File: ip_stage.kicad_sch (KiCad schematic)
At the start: 21 parts, among them J10 XH, J11 XH, U4 TL072

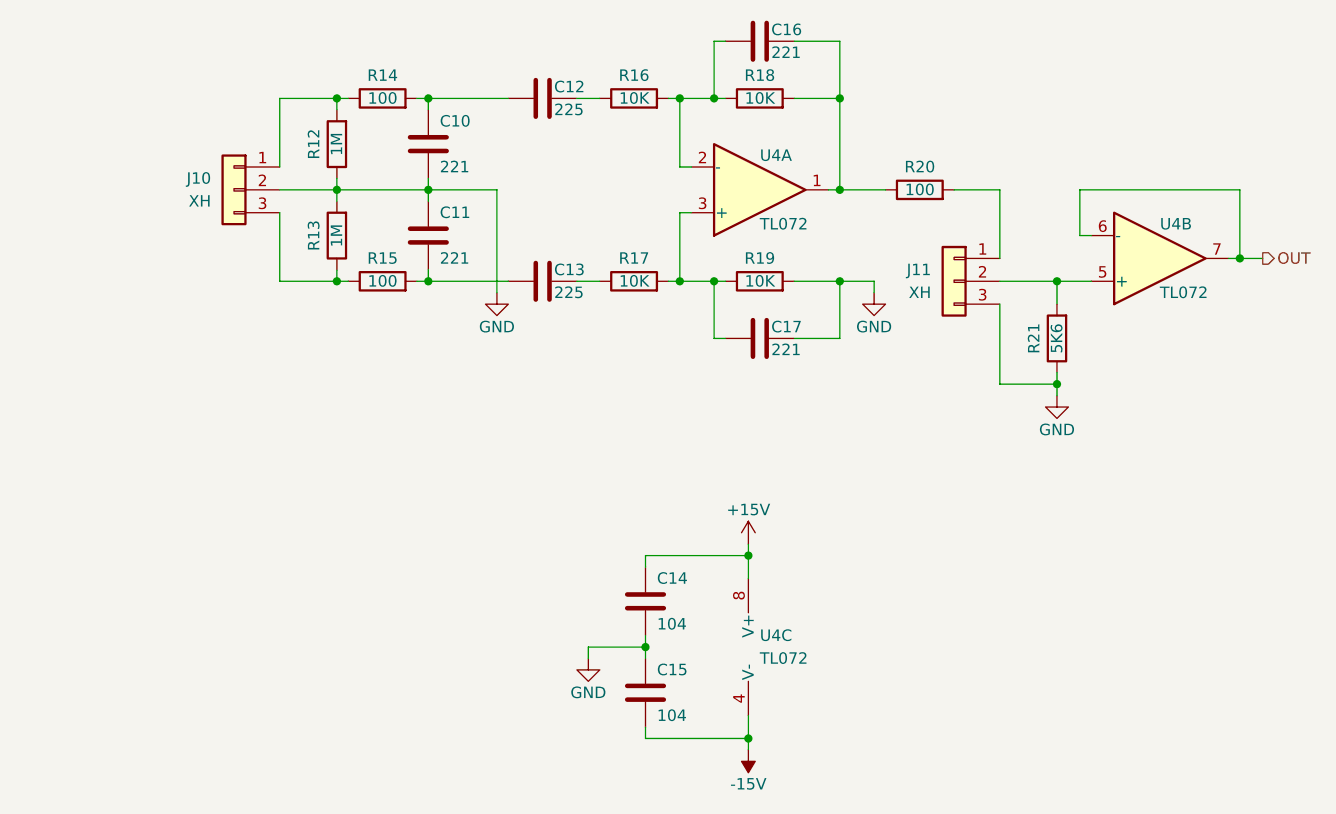
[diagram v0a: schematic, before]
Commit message: Added XLR input connectors for direct panel mounting. Added snap-off board for the level control pots with ribbon cable connection to the main board.
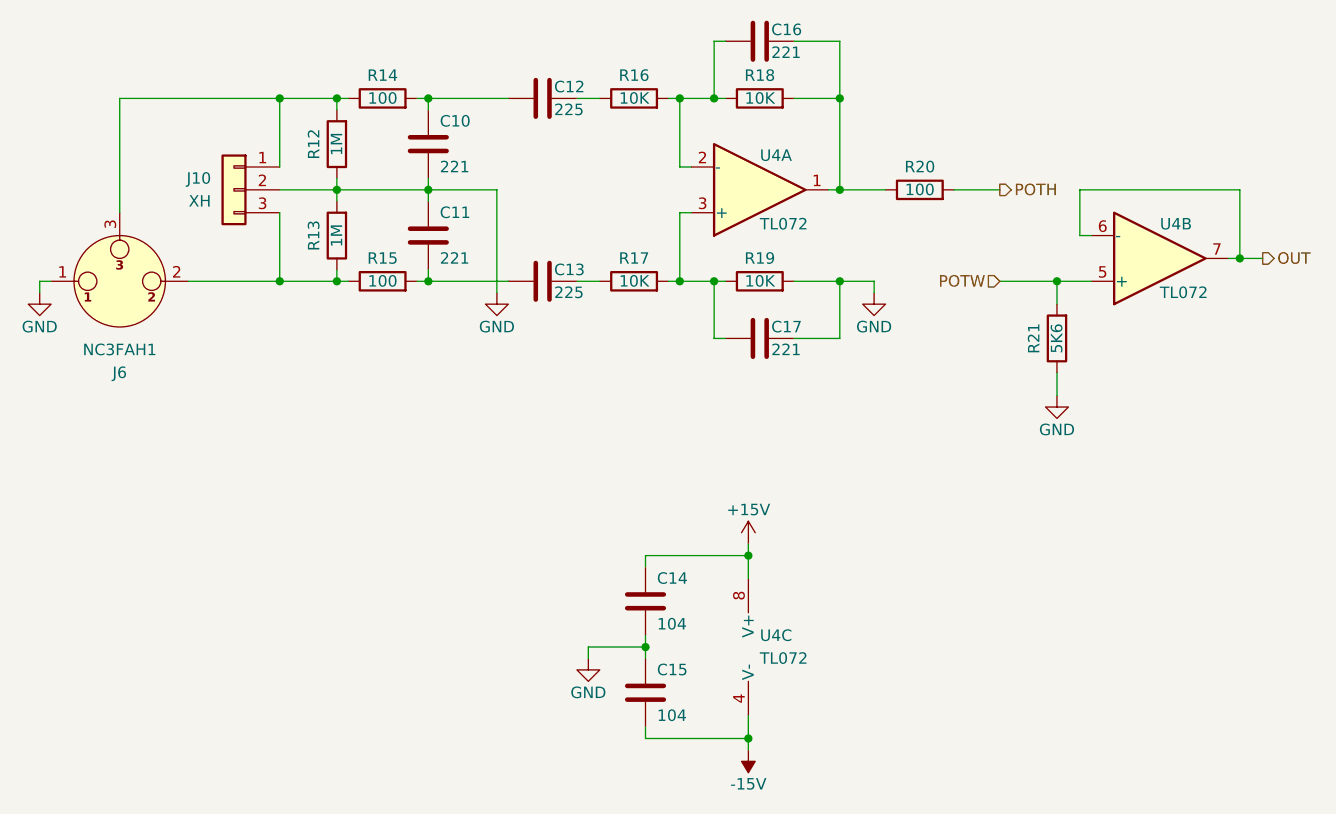
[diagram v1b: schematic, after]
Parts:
- removed J11: XH, Connector_JST:JST_XH_B3B-XH-AM_1x03_P2.50mm_Vertical, symbol Connector_Generic:Conn_01x03
- added J6: NC3FAH1, Connector_Audio:Jack_XLR_Neutrik_NC3FAH1_Horizontal, symbol Connector_Audio:NC3FAH1
- C12, C13: footprint Capacitor_SMD:C_1210_3225Metric -> Capacitor_THT:C_Rect_L10.3mm_W5.7mm_P7.50mm_MKS4
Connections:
- net GND: now also J6.1
- net at J10.1 (Pin_1), R12.2, R14.1: now also J6.3
- net at J10.3 (Pin_3), R13.1, R15.1: now also J6.2
- net POTW: now reaches R21.2, U4.5 (+)
- net POTH: now reaches R20.2
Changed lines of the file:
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@@
-	)
-	(junction
-		(at 158.75 85.09)
-		(diameter 0)
-		(color 0 0 0 0)
 	)
 	(junction
@@
 	)
 	(junction
+		(at 72.39 53.34)
+		(diameter 0)
+		(color 0 0 0 0)
+	)
+	(junction
 		(at 124.46 104.14)
+		(diameter 0)
+		(color 0 0 0 0)
+	)
+	(junction
+		(at 72.39 73.66)
 		(diameter 0)
 		(color 0 0 0 0)
@@
 	(wire
 		(pts
+			(xy 45.72 73.66) (xy 46.99 73.66)
+		)
+		(stroke
+			(width 0)
+			(type default)
+		)
+	)
+	(wire
+		(pts
 			(xy 134.62 63.5) (xy 139.7 63.5)
 		)
@@
 	(wire
 		(pts
-			(xy 152.4 71.12) (xy 152.4 63.5)
+			(xy 72.39 53.34) (xy 54.61 53.34)
 		)
 		(stroke
@@
 	(wire
 		(pts
-			(xy 158.75 85.09) (xy 158.75 83.82)
+			(xy 158.75 83.82) (xy 158.75 86.36)
 		)
 		(stroke
@@
 	(wire
 		(pts
-			(xy 152.4 76.2) (xy 152.4 85.09)
-		)
-		(stroke
-			(width 0)
-			(type default)
-		)
-	)
-	(wire
-		(pts
 			(xy 179.07 71.12) (xy 177.8 71.12)
 		)
@@
 	(wire
 		(pts
+			(xy 62.23 73.66) (xy 72.39 73.66)
+		)
+		(stroke
+			(width 0)
+			(type default)
+		)
+	)
+	(wire
+		(pts
 			(xy 161.29 63.5) (xy 179.07 63.5)
 		)
@@
 	(wire
 		(pts
-			(xy 152.4 85.09) (xy 158.75 85.09)
-		)
-		(stroke
-			(width 0)
-			(type default)
-		)
-	)
-	(wire
-		(pts
 			(xy 113.03 114.3) (xy 106.68 114.3)
 		)
@@
 	(wire
 		(pts
-			(xy 158.75 85.09) (xy 158.75 86.36)
-		)
-		(stroke
-			(width 0)
-			(type default)
-		)
-	)
-	(wire
-		(pts
 			(xy 134.62 46.99) (xy 129.54 46.99)
 		)
@@
 	(wire
 		(pts
+			(xy 54.61 53.34) (xy 54.61 66.04)
+		)
+		(stroke
+			(width 0)
+			(type default)
+		)
+	)
+	(wire
+		(pts
 			(xy 113.03 124.46) (xy 124.46 124.46)
 		)
@@
 		(pts
 			(xy 113.03 114.3) (xy 113.03 115.57)
+		)
+		(stroke
+			(width 0)
+			(type default)
+		)
+	)
+	(wire
+		(pts
+			(xy 45.72 74.93) (xy 45.72 73.66)
 		)
 		(stroke
@@
 			)
 			(justify left)
+		)
+	)
+	(hierarchical_label "POTH"
+		(shape output)
+		(at 152.4 63.5 0)
+		(effects
+			(font
+				(size 1.27 1.27)
+			)
+			(justify left)
+		)
+	)
+	(hierarchical_label "POTW"
+		(shape input)
+		(at 152.4 73.66 180)
+		(effects
+			(font
+				(size 1.27 1.27)
+			)
+			(justify right)
 		)
 	)
@@
 			)
 		)
-		(property "Footprint" "Capacitor_SMD:C_1210_3225Metric"
+		(property "Footprint" "Capacitor_THT:C_Rect_L10.3mm_W5.7mm_P7.50mm_MKS4"
 			(at 105.41 72.6948 0)
 			(effects
@@
 	)
 	(symbol
+		(lib_id "power:GND")
+		(at 45.72 74.93 0)
+		(unit 1)
+		(exclude_from_sim no)
+		(in_bom yes)
+		(on_board yes)
+		(dnp no)
+		(property "Reference" "#PWR7"
+			(at 45.72 81.28 0)
+			(effects
+				(font
+					(size 1.27 1.27)
+				)
+				(hide yes)
+			)
+		)
+		(property "Value" "GND"
+			(at 45.72 78.74 0)
+			(effects
+				(font
+					(size 1.27 1.27)
+				)
+			)
+		)
+		(property "Footprint" ""
+			(at 45.72 74.93 0)
+			(effects
+				(font
+					(size 1.27 1.27)
+				)
+				(hide yes)
+			)
+		)
+		(property "Datasheet" ""
+			(at 45.72 74.93 0)
+			(effects
+				(font
+					(size 1.27 1.27)
+				)
+				(hide yes)
+			)
+		)
+		(property "Description" "Power symbol creates a global label with name \"GND\" , ground"
+			(at 45.72 74.93 0)
+			(effects
+				(font
+					(size 1.27 1.27)
+				)
+				(hide yes)
+			)
+		)
+		(pin "1"
+		)
+		(instances
+			(project "0000.011D"
+				(path "/73c76ae1-0f6d-4072-b1f6-02bc5875bb36/18961242-887b-44bf-99d0-5f479ce4a18f"
+					(reference "#PWR7")
+					(unit 1)
+				)
+				(path "/73c76ae1-0f6d-4072-b1f6-02bc5875bb36/f110ea61-3f24-4cb4-b866-3cf7c5a9b206"
+					(reference "#PWR9")
+					(unit 1)
+				)
+			)
+		)
+	)
+	(symbol
 		(lib_id "Device:R")
 		(at 83.82 73.66 90)
@@
 			)
 		)
-		(property "Footprint" "Capacitor_SMD:C_1210_3225Metric"
+		(property "Footprint" "Capacitor_THT:C_Rect_L10.3mm_W5.7mm_P7.50mm_MKS4"
 			(at 105.41 52.3748 0)
 			(effects
@@
 	)
 	(symbol
-		(lib_id "Connector_Generic:Conn_01x03")
-		(at 147.32 73.66 0)
-		(mirror y)
+		(lib_id "Connector_Audio:NC3FAH1")
+		(at 54.61 73.66 0)
+		(mirror x)
 		(unit 1)
 		(exclude_from_sim no)
@@
 		(on_board yes)
 		(dnp no)
-		(property "Reference" "J11"
-			(at 144.78 72.3899 0)
-			(effects
-				(font
-					(size 1.27 1.27)
-				)
-				(justify left)
-			)
-		)
-		(property "Value" "XH"
-			(at 144.78 74.9299 0)
-			(effects
-				(font
-					(size 1.27 1.27)
-				)
-				(justify left)
-			)
-		)
-		(property "Footprint" "Connector_JST:JST_XH_B3B-XH-AM_1x03_P2.50mm_Vertical"
-			(at 147.32 73.66 0)
-			(effects
-				(font
-					(size 1.27 1.27)
-				)
-				(hide yes)
-			)
-		)
-		(property "Datasheet" "~"
-			(at 147.32 73.66 0)
-			(effects
-				(font
-					(size 1.27 1.27)
-				)
-				(hide yes)
-			)
-		)
-		(property "Description" "Generic connector, single row, 01x03, script generated (kicad-library-utils/schlib/autogen/connector/)"
-			(at 147.32 73.66 0)
-			(effects
-				(font
-					(size 1.27 1.27)
-				)
-				(hide yes)
-			)
+		(property "Reference" "J6"
+			(at 54.61 83.82 0)
+			(effects
+				(font
+					(size 1.27 1.27)
+				)
+			)
+		)
+		(property "Value" "NC3FAH1"
+			(at 54.61 81.28 0)
+			(effects
+				(font
+					(size 1.27 1.27)
+				)
+			)
+		)
+		(property "Footprint" "Connector_Audio:Jack_XLR_Neutrik_NC3FAH1_Horizontal"
+			(at 54.61 73.66 0)
+			(effects
+				(font
+					(size 1.27 1.27)
+				)
+				(hide yes)
+			)
+		)
+		(property "Datasheet" "https://www.neutrik.com/en/product/nc3fah1"
+			(at 54.61 73.66 0)
+			(effects
+				(font
+					(size 1.27 1.27)
+				)
+				(hide yes)
+			)
+		)
+		(property "Description" "A Series, 3 pole female XLR receptacle, grounding: mating connector shell to pin1 and front panel, horizontal PCB mount"
+			(at 54.61 73.66 0)
+			(effects
+				(font
+					(size 1.27 1.27)
+				)
+				(hide yes)
+			)
+		)
+		(pin "3"
+		)
+		(pin "1"
 		)
 		(pin "2"
 		)
-		(pin "3"
-		)
-		(pin "1"
-		)
 		(instances
-			(project "0000.011D"
+			(project ""
 				(path "/73c76ae1-0f6d-4072-b1f6-02bc5875bb36/18961242-887b-44bf-99d0-5f479ce4a18f"
-					(reference "J11")
+					(reference "J6")
 					(unit 1)
 				)
 				(path "/73c76ae1-0f6d-4072-b1f6-02bc5875bb36/f110ea61-3f24-4cb4-b866-3cf7c5a9b206"
-					(reference "J13")
-					(unit 1)
-				)
+					(reference "J8")
+					(unit 1)
+				)
